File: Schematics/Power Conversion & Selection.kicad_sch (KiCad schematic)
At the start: 8 parts, among them U603 TPS2117

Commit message: Add 5V power selection ckt
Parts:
- added C613, C614: 1u X7R 50V, Capacitor_SMD:C_0805_2012Metric, symbol Device:C
- added C615, C616: 2u2 X7R 50V, Capacitor_SMD:C_1206_3216Metric, symbol Device:C
- added R608, R609, R610: 10k 1%, Resistor_SMD:R_0402_1005Metric, symbol Device:R_Small
- added U604: TPS2117, Package_TO_SOT_SMD:SOT-583-8, symbol 0_Power_Multiplexers:TPS2117
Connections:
- net GND: now also C613.2, C614.2, C615.2, C616.2, R609.2, U604.1 (GND)
- net VIN1_THRESHOLD: now also R608.2, R609.1, U604.4 (PR1)
- net VOUT_SRC: now also R610.2, U604.8 (ST)
- net +3V3 renamed FMU_3V3
- new net +5V2_P2: C613.1, R608.1, U604.3 (VIN1), U604.5 (MODE)
- new net +VDD_5V: C615.1, C616.1, R610.1, U604.2 (VOUT), U604.7 (VOUT)
- new net VBUS: C614.1, U604.6 (VIN2)

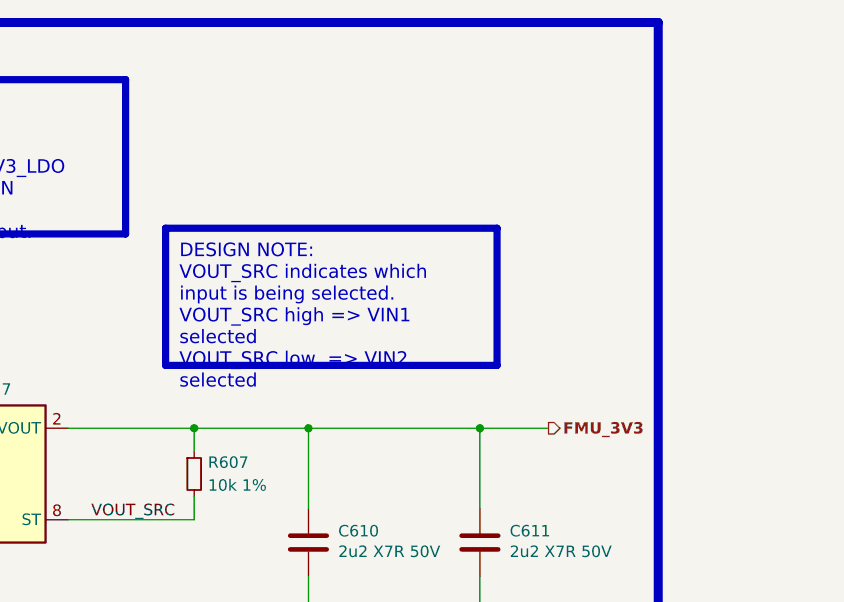
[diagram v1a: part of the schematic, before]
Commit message: Add FRAM
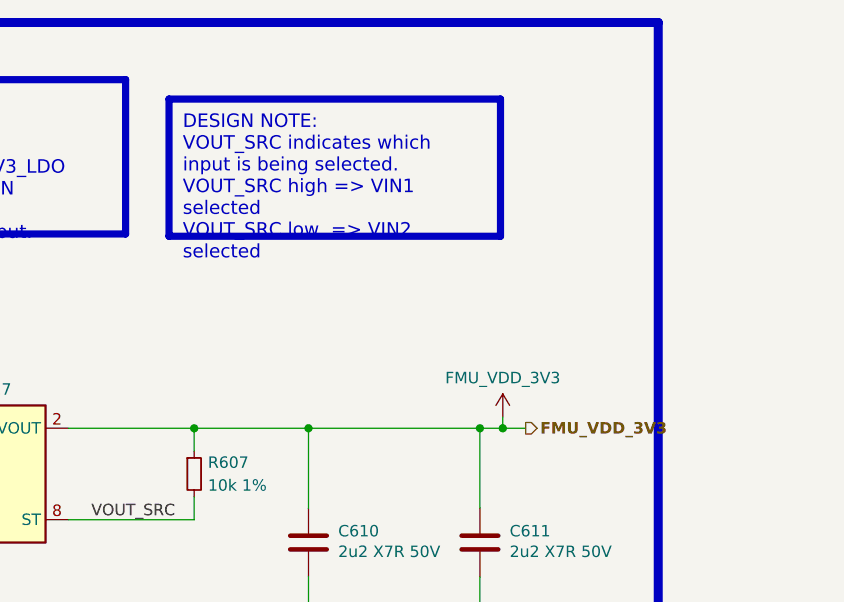
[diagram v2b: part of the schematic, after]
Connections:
- net FMU_3V3 renamed FMU_VDD_3V3
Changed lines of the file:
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@@
 	(text_box "DESIGN NOTE:\nVOUT_SRC indicates which input is being selected.\nVOUT_SRC high => VIN1 selected\nVOUT_SRC low  => VIN2 selected"
 		(exclude_from_sim no)
-		(at 144.145 159.385 0)
+		(at 144.526 145.034 0)
 		(size 36.83 15.24)
 		(margins 1.525 1.525 1.525 1.525)
@@
 	)
 	(junction
+		(at 181.61 181.61)
+		(diameter 0)
+		(color 0 0 0 0)
+	)
+	(junction
 		(at 160.02 181.61)
 		(diameter 0)
@@
 	)
 	(junction
+		(at 107.95 181.61)
+		(diameter 0)
+		(color 0 0 0 0)
+	)
+	(junction
 		(at 179.07 181.61)
 		(diameter 0)
@@
 	)
 	(junction
-		(at 107.95 181.61)
-		(diameter 0)
-		(color 0 0 0 0)
-	)
-	(junction
 		(at 160.02 207.01)
 		(diameter 0)
@@
 		(pts
 			(xy 107.95 165.1) (xy 107.95 181.61)
+		)
+		(stroke
+			(width 0)
+			(type default)
+		)
+	)
+	(wire
+		(pts
+			(xy 181.61 180.34) (xy 181.61 181.61)
 		)
 		(stroke
@@
 	(wire
 		(pts
+			(xy 181.61 181.61) (xy 184.15 181.61)
+		)
+		(stroke
+			(width 0)
+			(type default)
+		)
+	)
+	(wire
+		(pts
 			(xy 340.36 198.12) (xy 340.36 207.01)
 		)
@@
 	(wire
 		(pts
-			(xy 179.07 181.61) (xy 186.69 181.61)
+			(xy 179.07 181.61) (xy 181.61 181.61)
 		)
 		(stroke
@@
 		)
 	)
-	(hierarchical_label "FMU_3V3"
+	(hierarchical_label "FMU_VDD_3V3"
 		(shape output)
-		(at 186.69 181.61 0)
+		(at 184.15 181.61 0)
 		(effects
 			(font
@@
 					(unit 1)
 				)
+			)
+		)
+	)
+	(symbol
+		(lib_id "power:+5V")
+		(at 181.61 180.34 0)
+		(unit 1)
+		(body_style 1)
+		(exclude_from_sim no)
+		(in_bom yes)
+		(on_board yes)
+		(in_pos_files yes)
+		(dnp no)
+		(property "Reference" "#PWR0308"
+			(at 181.61 184.15 0)
+			(hide yes)
+			(show_name no)
+			(do_not_autoplace no)
+			(effects
+				(font
+					(size 1.27 1.27)
+				)
+			)
+		)
+		(property "Value" "FMU_VDD_3V3"
+			(at 181.61 176.022 0)
+			(show_name no)
+			(do_not_autoplace no)
+			(effects
+				(font
+					(size 1.27 1.27)
+				)
+			)
+		)
+		(property "Footprint" ""
+			(at 181.61 180.34 0)
+			(hide yes)
+			(show_name no)
+			(do_not_autoplace no)
+			(effects
+				(font
+					(size 1.27 1.27)
+				)
+			)
+		)
+		(property "Datasheet" ""
+			(at 181.61 180.34 0)
+			(hide yes)
+			(show_name no)
+			(do_not_autoplace no)
+			(effects
+				(font
+					(size 1.27 1.27)
+				)
+			)
+		)
+		(property "Description" "Power symbol creates a global label with name \"+5V\""
+			(at 181.61 180.34 0)
+			(hide yes)
+			(show_name no)
+			(do_not_autoplace no)
+			(effects
+				(font
+					(size 1.27 1.27)
+				)
+			)
+		)
+		(pin "1"
+		)
+		(instances
+			(project "SkyForge_Controller"
+				(path "/0650c7a8-acba-429c-9f8e-eec0baf0bc1c/fede4c36-00cc-4d3d-b71c-5243ba232202/021f90fa-490d-4e3b-988d-faee877a382b"
+					(reference "#PWR0308")
+					(unit 1)
+				)
